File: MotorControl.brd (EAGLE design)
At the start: 69 x 57 mm, 47 parts, among them IC1 ESP32-WROOM-32E8M, IC2 TB6612FNG, U3 TP4056, U4 SPX3940AM3-L-3-3/TR, U5 INTERFACE-FT230XS-R(SSOP16)

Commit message: [fix] シルク作成
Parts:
- removed C17: 4.7uf, OPL_Capacitor:AVX-A
- added C1: 100nf, OPL_Capacitor:C0805
- C10: value 100nF/50V(10%) -> 4.7uf; device OPL_Capacitor:C0603 -> OPL_Capacitor:AVX-A
- C2: value 100nf -> 10uf; device OPL_Capacitor:C0805 -> OPL_Capacitor:C1206
- C3: value 10uf -> 22uF/16V(10%)
- C4: value 22uF/16V(10%) -> 100nf; device OPL_Capacitor:C1206 -> OPL_Capacitor:C0805
- C5: value 100nf -> 10nf
- C6: value 10nf -> 100nF/50V(10%); device OPL_Capacitor:C0805 -> OPL_Capacitor:C0603
- moved C2 47.5 mm to (3.54, 22.6), turned to 270 degrees
- moved C6 46.5 mm to (19.8, 41.6), turned to 180 degrees
- moved C10 40.4 mm to (59.1, 27.6)
- moved C4 39.9 mm to (51.5, 42.9)
- moved C5 28.4 mm to (58.1, 15.2), turned to 0 degrees
- moved C3 17.4 mm to (12.0, 37.8), turned to 90 degrees
- moved C7 5.08 mm to (19.8, 36.5), turned to 0 degrees
- renumbered BOOT_SW to BOOT-SW, D1 to BAT-RED, D2 to USB-TO-SERIAL-LED, D3 to PWR-LED, D4 to BAT-BLUE, E1 to FERRITE-BEAD, F1 to HUSE, IC1 to ESP32, IC2 to DRIVER-IC, MOTOR_PIN to MOTOR-PIN, POWER_SW to PWR-SW, R13 to R5, U3 to CHARGER-IC, U4 to LDO-IC, U5 to CNV-IC
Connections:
- net +3V3: now also C3.2, C6.2; no longer C4.2, C7.2
- net B+: now also C2.2; no longer C3.2
- net GND: now also C1.1, C10.-, C5.2, C6.1; no longer C10.1, C17.-, C5.1, C6.2
- net N$19: now also C10.+; no longer C17.+
- net N$29: now also C7.2; no longer C10.2
- net N$5: now also C4.2; no longer C5.2
- net VBUS: now also C5.1; no longer C6.1
- net VIN+: now also C1.2; no longer C2.2
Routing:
- net GND: track 310.3 -> 295.1 mm, vias 31 -> 30
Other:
- board text added: "+"
- board text added: "-"
- board text added: "AO1"
- board text added: "AO2"
- board text added: "BO1"
- board text added: "BO2"

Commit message: [Fix] 20210920MT時点（４層）
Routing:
- net GND: track 295.1 -> 310.8 mm
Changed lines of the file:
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@@
 <setting verticaltext="up"/>
 </settings>
-<grid distance="1" unitdist="mm" unit="mm" style="lines" multiple="1" display="yes" altdistance="0.25" altunitdist="mm" altunit="mm"/>
+<grid distance="1" unitdist="mm" unit="mm" style="lines" multiple="1" display="yes" altdistance="5" altunitdist="mil" altunit="mil"/>
 <layers>
 <layer number="1" name="Top" color="4" fill="1" visible="yes" active="yes"/>
@@
 <element name="PWR-LED" library="OPL_Optoelectronics" package="LED-0805" package3d_urn="urn:adsk.eagle:package:8004829/1" value="YELLOW-0805" x="33.21" y="3.59" smashed="yes">
 <attribute name="MPN" value="17-215UYC/S530-A3/TR8" x="94.17" y="-56.1" size="1.778" layer="27" display="off"/>
-<attribute name="NAME" x="30.805" y="4.983" size="0.8128" layer="25" ratio="11"/>
+<attribute name="NAME" x="32.055" y="1.233" size="0.8128" layer="25" ratio="11"/>
 </element>
 <element name="BAT-BLUE" library="OPL_Optoelectronics" package="LED-0805" package3d_urn="urn:adsk.eagle:package:8004829/1" value="CLEAR-BLUE-0805" x="42.64" y="20.02" smashed="yes" rot="R270">
@@
 </element>
 <element name="HUSE" library="SMD0805R035SF" package="SMD0805R035SF" value="SMD0805R035SF" x="65.5" y="23.83" smashed="yes">
-<attribute name="NAME" x="63.5" y="21.08" size="1.016" layer="27"/>
+<attribute name="NAME" x="59.75" y="21.83" size="1.016" layer="27"/>
 </element>
 <element name="ESP32" library="ESP32-WROOM-32" library_urn="urn:adsk.eagle:library:30575316" package="ESP32WROOM32E8MB" package3d_urn="urn:adsk.eagle:package:30670992/1" value="ESP32-WROOM-32E8M" x="33.75" y="40.34" smashed="yes">
@@
 <element name="R11" library="OPL_Resistor" package="R0805" package3d_urn="urn:adsk.eagle:package:8004935/1" value="27R" x="60.42" y="42.88" smashed="yes" rot="R270">
 <attribute name="MPN" value="RC0805JR-071KL" x="-4.35" y="-6.65" size="1.778" layer="27" rot="R270" display="off"/>
-<attribute name="NAME" x="61.325" y="41.364" size="0.8128" layer="25" font="vector" ratio="11" rot="R180"/>
+<attribute name="NAME" x="61.325" y="41.364" size="0.8128" layer="25" ratio="11" rot="R180"/>
 </element>
 <element name="R12" library="OPL_Resistor" package="R0805" package3d_urn="urn:adsk.eagle:package:8004935/1" value="0.1R" x="47.72" y="22.56" smashed="yes" rot="R180">
@@
 <wire x1="13.8778" y1="19.812" x2="13.97" y2="19.75" width="0.9144" layer="1"/>
 <wire x1="3.6416" y1="24.1046" x2="7.40715" y2="20.33905" width="0.9144" layer="16"/>
-<wire x1="9.4201" y1="15.5194" x2="9.493" y2="15.448" width="0.9144" layer="1"/>
 <wire x1="3.6416" y1="24.1046" x2="3.54" y2="24.211" width="0.9144" layer="1"/>
 <wire x1="12.557" y1="30.3784" x2="12.7" y2="30.339" width="0.9144" layer="1"/>
-<wire x1="12.0617" y1="35.9918" x2="11.97" y2="36.149" width="0.9144" layer="1"/>
 <wire x1="3.6416" y1="35.9918" x2="2.4859" y2="35.9918" width="0.9144" layer="1"/>
 <wire x1="2.4859" y1="35.9918" x2="2.461" y2="35.849" width="0.9144" layer="1"/>
-<wire x1="9.5852" y1="36.322" x2="11.5664" y2="36.322" width="0.9144" layer="1"/>
-<wire x1="11.5664" y1="36.322" x2="11.97" y2="36.149" width="0.9144" layer="1"/>
 <wire x1="3.6416" y1="25.4254" x2="3.6416" y2="24.5999" width="0.9144" layer="1"/>
 <wire x1="4.1369" y1="25.9207" x2="3.6416" y2="25.4254" width="0.9144" layer="16"/>
@@
 <wire x1="3.6416" y1="24.5999" x2="3.54" y2="24.211" width="0.9144" layer="1"/>
 <wire x1="3.8067" y1="35.6616" x2="3.6416" y2="35.9918" width="0.9144" layer="1"/>
-<wire x1="62.4172" y1="14.1986" x2="58.1246" y2="14.1986" width="0.9144" layer="16"/>
-<wire x1="58.1246" y1="14.1986" x2="58.07" y2="14.321" width="0.9144" layer="1"/>
+<wire x1="58.1246" y1="14.1986" x2="62" y2="14.1986" width="0.9144" layer="16"/>
 <wire x1="40.2938" y1="3.7973" x2="40.2938" y2="4.4577" width="0.9144" layer="16"/>
 <wire x1="40.9542" y1="3.1369" x2="40.2938" y2="3.7973" width="0.9144" layer="16"/>
@@
 <wire x1="40.2938" y1="4.4577" x2="40.275" y2="4.55" width="0.9144" layer="1"/>
 <wire x1="42.7703" y1="4.4577" x2="42.815" y2="4.55" width="0.9144" layer="1"/>
-<wire x1="50.8602" y1="5.7785" x2="50.8602" y2="7.4295" width="0.9144" layer="16"/>
+<wire x1="50.8602" y1="7.4295" x2="50.8602" y2="5.7785" width="0.9144" layer="16"/>
 <wire x1="50.8602" y1="7.4295" x2="50.8602" y2="9.0805" width="0.9144" layer="16"/>
-<wire x1="52.181" y1="4.4577" x2="50.8602" y2="5.7785" width="0.9144" layer="16"/>
 <wire x1="50.8602" y1="9.0805" x2="50.752" y2="9.13" width="0.9144" layer="1"/>
 <wire x1="52.3461" y1="2.8067" x2="51.3555" y2="1.8161" width="0.9144" layer="16"/>
@@
 <wire x1="57.8" y1="7.41" x2="57.7944" y2="7.4295" width="0.9144" layer="1"/>
 <wire x1="66.0494" y1="11.2268" x2="66.0494" y2="9.0805" width="0.9144" layer="16"/>
-<wire x1="58.1246" y1="7.7597" x2="57.8" y2="7.41" width="0.9144" layer="1"/>
 <wire x1="61.2615" y1="31.8643" x2="60.436" y2="31.0388" width="0.9144" layer="16"/>
 <wire x1="61.2615" y1="32.6898" x2="61.2615" y2="31.8643" width="0.9144" layer="16"/>
@@
 <wire x1="55.54015" y1="40.06215" x2="59.23115" y2="36.37115" width="0.9144" layer="16"/>
 <wire x1="59.23115" y1="36.37115" x2="61.2615" y2="34.3408" width="0.9144" layer="16"/>
-<wire x1="61.2615" y1="33.1851" x2="61.309" y2="32.72" width="0.9144" layer="1"/>
 <wire x1="62.7474" y1="25.0952" x2="64.3984" y2="23.4442" width="0.9144" layer="16"/>
 <wire x1="59.4454" y1="21.9583" x2="18.0053" y2="21.9583" width="0.9144" layer="16"/>
@@
 <wire x1="53.34" y1="44.45" x2="53.9971" y2="43.7929" width="0.8636" layer="16"/>
 <wire x1="53.9971" y1="43.7929" x2="53.9971" y2="41.6052" width="0.8636" layer="16"/>
-<wire x1="61.69" y1="37.3375" x2="61.1825" y2="36.83" width="0.3556" layer="1"/>
-<wire x1="60.96" y1="36.83" x2="61.1825" y2="36.83" width="0.3556" layer="1"/>
-<wire x1="60.50115" y1="36.37115" x2="60.96" y2="36.83" width="0.3556" layer="1"/>
-<wire x1="60.50115" y1="36.37115" x2="59.23115" y2="36.37115" width="0.3556" layer="1"/>
+<wire x1="61.69" y1="37.3375" x2="60.72365" y2="36.37115" width="0.3556" layer="1"/>
+<wire x1="60.72365" y1="36.37115" x2="59.23115" y2="36.37115" width="0.3556" layer="1"/>
 <wire x1="60.42" y1="27.64" x2="60.72" y2="27.94" width="0.9144" layer="1"/>
 <wire x1="60.72" y1="27.94" x2="62.23" y2="27.94" width="0.9144" layer="16"/>
@@
 <wire x1="62.23" y1="27.94" x2="62.23" y2="25.6126" width="0.9144" layer="16"/>
 <wire x1="62.23" y1="25.6126" x2="62.7474" y2="25.0952" width="0.9144" layer="16"/>
-<via x="58.1246" y="14.1986" extent="1-16" drill="0.35"/>
 <wire x1="64.4" y1="12.13" x2="65.1462" y2="12.13" width="0.9144" layer="16"/>
 <wire x1="65.1462" y1="12.13" x2="66.0494" y2="11.2268" width="0.9144" layer="16"/>
@@
 <via x="4.1369" y="35.3314" extent="1-16" drill="0.35"/>
 <via x="3.6416" y="25.4254" extent="1-16" drill="0.35"/>
-<via x="9.5852" y="36.322" extent="1-16" drill="0.35"/>
+<via x="9.5852" y="35.322" extent="1-16" drill="0.35"/>
 <via x="12.557" y="30.3784" extent="1-16" drill="0.35"/>
 <via x="18.9959" y="37.3126" extent="1-16" drill="0.35"/>
-<wire x1="9.5852" y1="36.322" x2="9.5852" y2="33.3502" width="0.8636" layer="16"/>
+<wire x1="9.5852" y1="35.322" x2="9.5852" y2="33.3502" width="0.8636" layer="16"/>
 <wire x1="9.5852" y1="33.3502" x2="12.557" y2="30.3784" width="0.8636" layer="16"/>
 <wire x1="6.779" y1="40.291" x2="6.779" y2="40.211" width="0.8636" layer="1"/>
-<wire x1="9.5852" y1="37.4048" x2="9.5852" y2="36.322" width="0.8636" layer="1"/>
+<wire x1="9.5852" y1="37.4048" x2="9.5852" y2="35.322" width="0.8636" layer="1"/>
 <wire x1="6.779" y1="40.211" x2="9.5852" y2="37.4048" width="0.8636" layer="1"/>
 <wire x1="6.779" y1="40.291" x2="6.779" y2="39.1292" width="0.8636" layer="1"/>
@@
 <vertex x="68" y="56"/>
 </polygon>
+<wire x1="11.97" y1="36.149" x2="10.841" y2="36.149" width="0.8636" layer="1"/>
+<wire x1="10.841" y1="36.149" x2="9.5852" y2="37.4048" width="0.8636" layer="1"/>
+<wire x1="52.3461" y1="4.2926" x2="52.3461" y2="2.8067" width="0.8636" layer="16"/>
+<wire x1="62" y1="14.1986" x2="62.3314" y2="14.1986" width="0.8636" layer="16"/>
+<wire x1="62.3314" y1="14.1986" x2="64.4" y2="12.13" width="0.8636" layer="16"/>
+<wire x1="64.3984" y1="23.4442" x2="64.3984" y2="16.597" width="0.8636" layer="16"/>
+<wire x1="64.3984" y1="16.597" x2="62" y2="14.1986" width="0.8636" layer="16"/>
+<wire x1="50.8602" y1="5.7785" x2="52.3461" y2="4.2926" width="0.8636" layer="16"/>
+<wire x1="58.07" y1="14.321" x2="58.07" y2="13.05" width="0.8636" layer="1"/>
+<wire x1="58.07" y1="13.05" x2="58.42" y2="12.7" width="0.8636" layer="1"/>
+<via x="58.42" y="12.7" extent="1-16" drill="0.35"/>
 </signal>
 <signal name="AO1" class="2">

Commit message: [Modify] 部品置換前。在庫チェック中
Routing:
- net GND: track 310.8 -> 231.5 mm, vias 30 -> 3
- net VBUS: track 43.4 -> 12.0 mm
- net B+: track 107.3 -> 130.9 mm, vias 2 -> 3
- net BO2: track 18.8 -> 0.00 mm, vias 1 -> 0
- net RXD: track 17.4 -> 0.00 mm, vias 2 -> 0
- net BIN2: track 35.2 -> 18.0 mm
- net N$8: track 13.3 -> 0.00 mm, vias 2 -> 0
- net AO2: track 13.2 -> 0.00 mm, vias 1 -> 0
- net VIN+: track 65.9 -> 77.6 mm, vias 2 -> 3
- net N$7: track 11.3 -> 0.00 mm, vias 2 -> 0
- net N$3: track 75.8 -> 86.6 mm, vias 2 -> 0
- net N$9: track 13.9 -> 3.72 mm
- net N$19: track 43.4 -> 33.9 mm, vias 4 -> 2
- net N$15: track 13.1 -> 4.80 mm, vias 2 -> 0
- net N$6: track 7.31 -> 0.00 mm
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- removed copper zone on layer 16, net GND

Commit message: [M] ２面に対応
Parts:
- removed R12, R9: 0.1R, OPL_Resistor:R0805
- added C17: 10UF 6.3V, OPL_Capacitor:C0603
- added IC1: DW01A, DW01A:SOT23-6
- added Q1: FS8205A, FS8205A:SOP65P640X120-8N
- C13: value 10uf -> 100nf
- R5: value 0.1R -> 100R; device OPL_Resistor:R0805 -> OPL_Resistor:R1206
- R8: value 0.1R -> 1K
- moved C13 46.9 mm to (57.1, 19.1), turned to 270 degrees
- moved C10 14.2 mm to (65.5, 40.3)
- moved C16 12.5 mm to (65.5, 44.1)
- moved FERRITE-BEAD 10.9 mm to (57.9, 40.3)
- moved C15 8.89 mm to (61.7, 46.7), turned to 180 degrees
- moved R11 4.58 mm to (56.6, 45.4), turned to 0 degrees
- moved R8 3.28 mm to (49.5, 19.1), turned to 0 degrees
- moved R5 2.05 mm to (49.5, 26.7), turned to 180 degrees
- moved C4 1.80 mm to (50.3, 44.1)
- moved R7 1.27 mm to (50.3, 12.4), turned to 180 degrees
- moved R10 1.27 mm to (50.3, 49.2)
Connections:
- removed net N$17: R8.2, R9.1
- removed net N$20: R12.2, R5.1
- new net B-: BAT.-, C13.2, IC1.6, Q1.2, Q1.3
- new net N$1: IC1.3, Q1.5
- new net N$10: IC1.1, Q1.4
- net B+: now also C17.1, R5.2; no longer C13.2
- net GND: now also C17.2, Q1.6, Q1.7, R8.2; no longer BAT.-, C13.1
- net N$18: now also C13.1, IC1.5, R5.1; no longer R12.1, R9.2
- net N$19: now also IC1.2; no longer C10.+, C16.2, CNV-IC.12, FERRITE-BEAD.1, R7.2
- net VIN+: now also C10.+, C16.2, CNV-IC.12, FERRITE-BEAD.1, R7.2; no longer R5.2
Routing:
- net GND: track 231.5 -> 319.3 mm, vias 3 -> 14
- net B-: track 0.00 -> 35.1 mm, vias 0 -> 3
- net RXD: track 0.00 -> 33.3 mm, vias 0 -> 2
- net VBUS: track 12.0 -> 41.6 mm, vias 0 -> 2
- net N$19: track 33.9 -> 9.02 mm
- net B+: track 130.9 -> 155.3 mm, vias 3 -> 4
- net VIN+: track 77.6 -> 101.8 mm, vias 3 -> 6
- net BIN2: track 18.0 -> 36.9 mm
- net BO2: track 0.00 -> 18.2 mm, vias 0 -> 1
- net N$1: track 0.00 -> 14.5 mm, vias 0 -> 2
- net N$18: track 5.07 -> 19.5 mm, vias 0 -> 2
- net N$10: track 0.00 -> 14.3 mm
- net AO2: track 0.00 -> 13.2 mm, vias 0 -> 1
- net N$8: track 0.00 -> 12.6 mm
- net N$7: track 0.00 -> 11.0 mm
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- added copper zone on layer 1, net GND
- added copper zone on layer 16, net GND

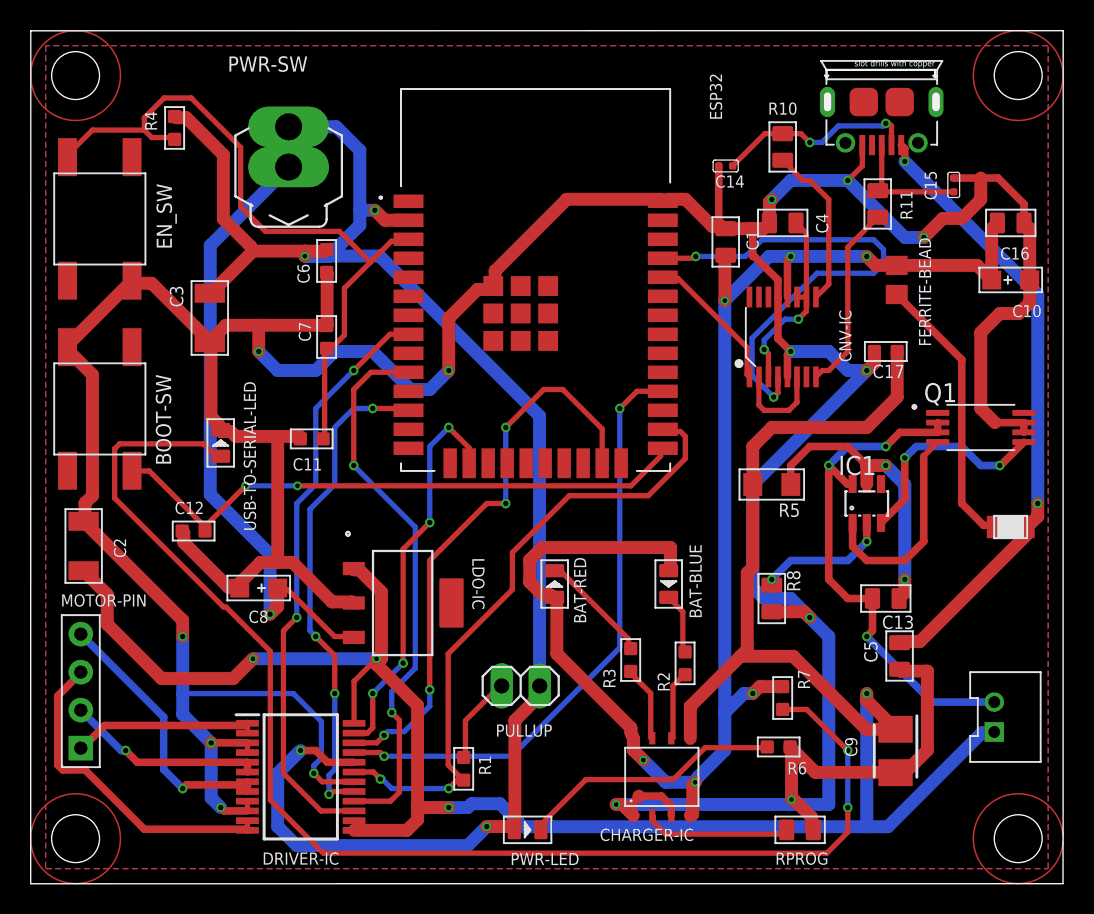
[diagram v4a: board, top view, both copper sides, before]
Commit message: [A] add output data
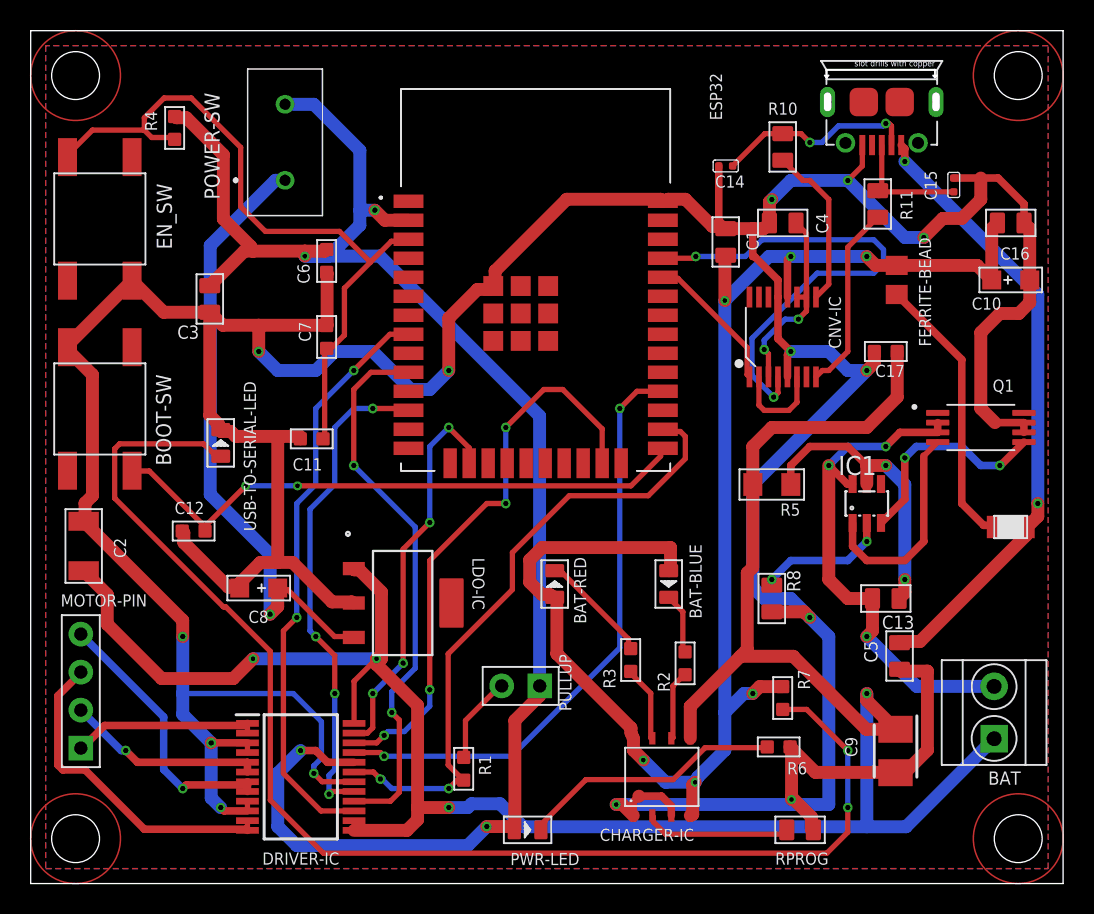
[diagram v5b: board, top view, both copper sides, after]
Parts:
- removed PWR-SW: (no value), switch:MS243
- added POWER-SW: A11JP, A11JP:A11JP
- BAT: value 2p-2.0 -> GREEN-2P-3.5; device OPL_Connector:H2-2.0-6X4.5MM -> OPL_Connector:H2-3.5-7.0X7.0MM
- C3: value 22uF/16V(10%) -> 22uf; device OPL_Capacitor:C1206 -> OPL_Capacitor:C0805
- PULLUP: device pinhead:1X02 -> OPL_Connector:H2-2.54
- moved C3 1.27 mm to (12.0, 39.1), turned to 180 degrees
- moved BAT 0.82 mm to (64.4, 11.4)
- turned PULLUP to 270 degrees
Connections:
- net +3V3: now also POWER-SW.3; no longer PWR-SW.2
- net B+: now also BAT.1; no longer BAT.+
- net B-: now also BAT.2; no longer BAT.-
- net POWER_SW: now also POWER-SW.1; no longer PWR-SW.1
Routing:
- net GND: track 319.3 -> 320.3 mm
- net +3V3: track 114.4 -> 115.1 mm
- net POWER_SW: track 42.2 -> 41.6 mm
